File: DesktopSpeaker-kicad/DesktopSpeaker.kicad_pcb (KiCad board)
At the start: 4 copper layers, 127.5 x 137.6 mm, 360 parts, among them J1 USB_C_Receptacle_USB2.0_16P, J10 B2P-VH, J11 B2P-VH, J2 HEAD_OUT, J3 AUX_IN, J4 I2C service, J5 1S_PACK_3PIN, J6 SWD, J7 SWD_TC2030, J8 BM83_PROG, J9 B2P-VH, Q100 2N7002, Q101 2N7002, Q102 2N7002, Q103 CSD17579Q3A, Q104 2N7002, SW100 WAKE_QON, SW101 BAT_DISCONNECT, SW102 EC11E, U1 BM83SM1-00TA, U10 TPA6132A2RTER, U11 TPS25730DREFR, U12 TPS7A0230PDBVR, U13 TS5A3167DBVR, U14 TPS63802DLAR, U15 TPS63802DLAR, U16 TS5A3167DBVR, U17 TS5A3167DBVR, U19 TPS7B8450QWDRBRQ1, U2 PCM2902CDBR, U20 TPS2116DRLR, U21 TPS3839G33DBZR, U22 TPS7A2033PDBVR, U23 TPS22917DBVR, U24 PCM1862DBTR, U25 TPS61088RHLR, U3 STM32G071RBT6, U4 BQ25792RQMR, U5 MAX17048G+T10, U6 TAS5825MRHBR, U7 TAS5825MRHBR, U8 TS5A23157DGSR, U9 TS5A23157DGSR, Y170 12MHz, Y200 24.576MHz

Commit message: R6o adopted: DRC 0/0 (silk cleared, USB FS waiver rule, audio GND vias), library silk fixes, ignore intermediate boards
Co-Authored-By: Claude Fable 5.1 <noreply@anthropic.com>
Claude-Session: https://claude.ai/code/session_016fe4xPJbEE2SjGafuyNLjb
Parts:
- moved LOGO1 80.0 mm to (173.2, 55.1)
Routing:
- net /3V3_AUDIO: track 299.6 -> 301.9 mm
- net GND: vias 270 -> 272

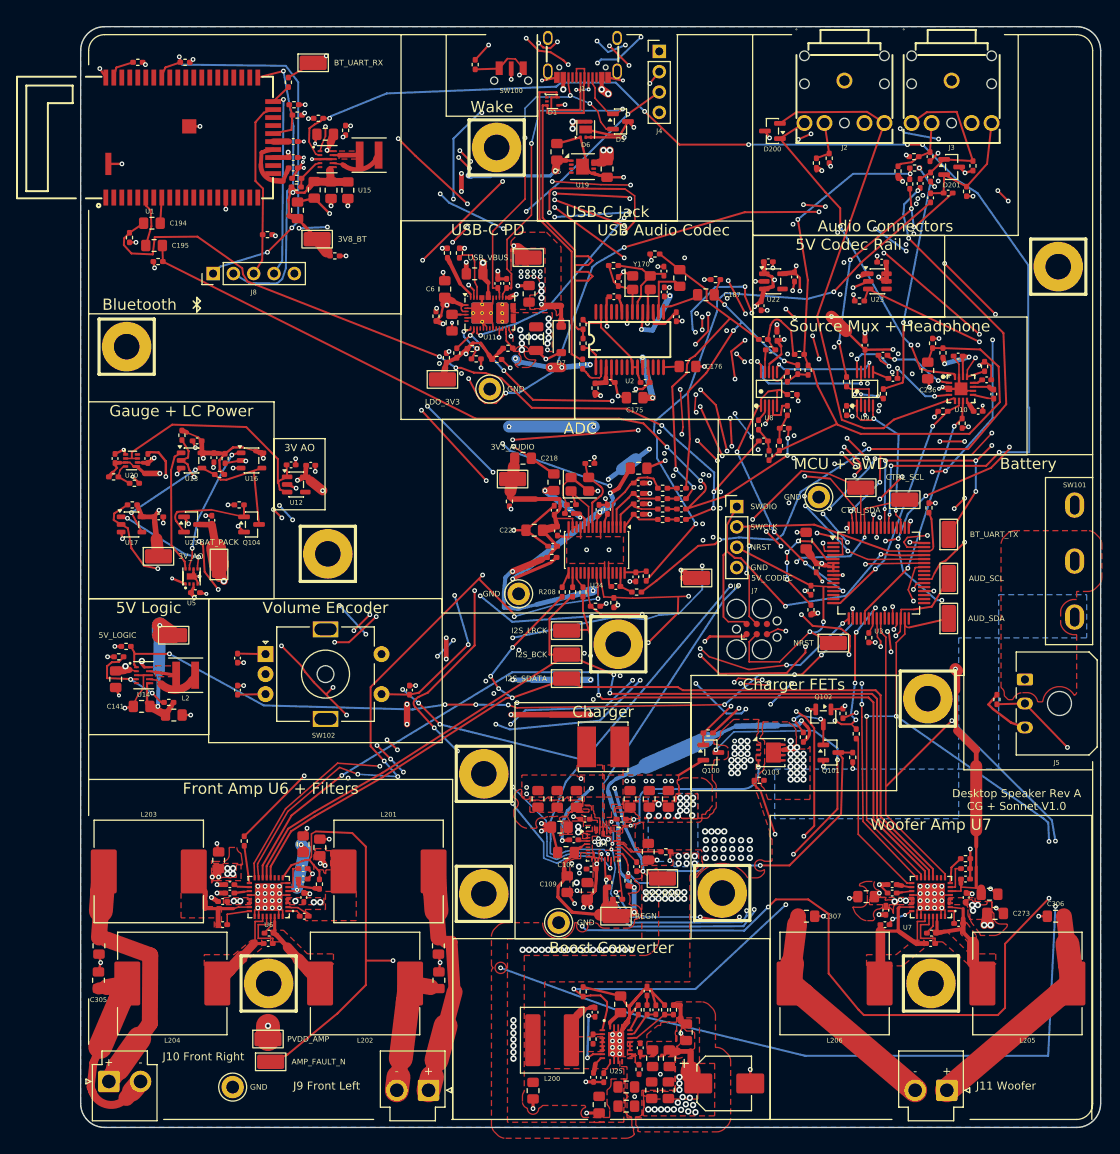
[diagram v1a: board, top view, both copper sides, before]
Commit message: R6p adopted: slow-signal geometry cleanup (16 nets shortened, -75 vias), teardrop strip/prune tools, fab export helper
- Project board = R6p-final: DRC 0/0, 0 open edges, USB/I2S copper and footprints unchanged vs R6o; rules unchanged.
- GUI teardrop pass of 2026-10-11 stripped (stale fills caused the 499 clearance items); U14-L2 GUI polyline redraw reverted to the 1.0 mm arc; td_curve_segcount back to 5.
- helpers: route_td_strip.py, route_td_prune.py, route_r6p_geom/improve/cucmp/netsvg/try/dangle.py, fab_export.sh (gerbers, drills, JLC CPL).
- .gitignore: KiCad local history, stray plugin log, work-r6 prl files, R6p finals tracked.
- Handover: R6p update and revised remaining fab steps.

Co-Authored-By: Claude Fable 5.1 <noreply@anthropic.com>
Claude-Session: https://claude.ai/code/session_016fe4xPJbEE2SjGafuyNLjb
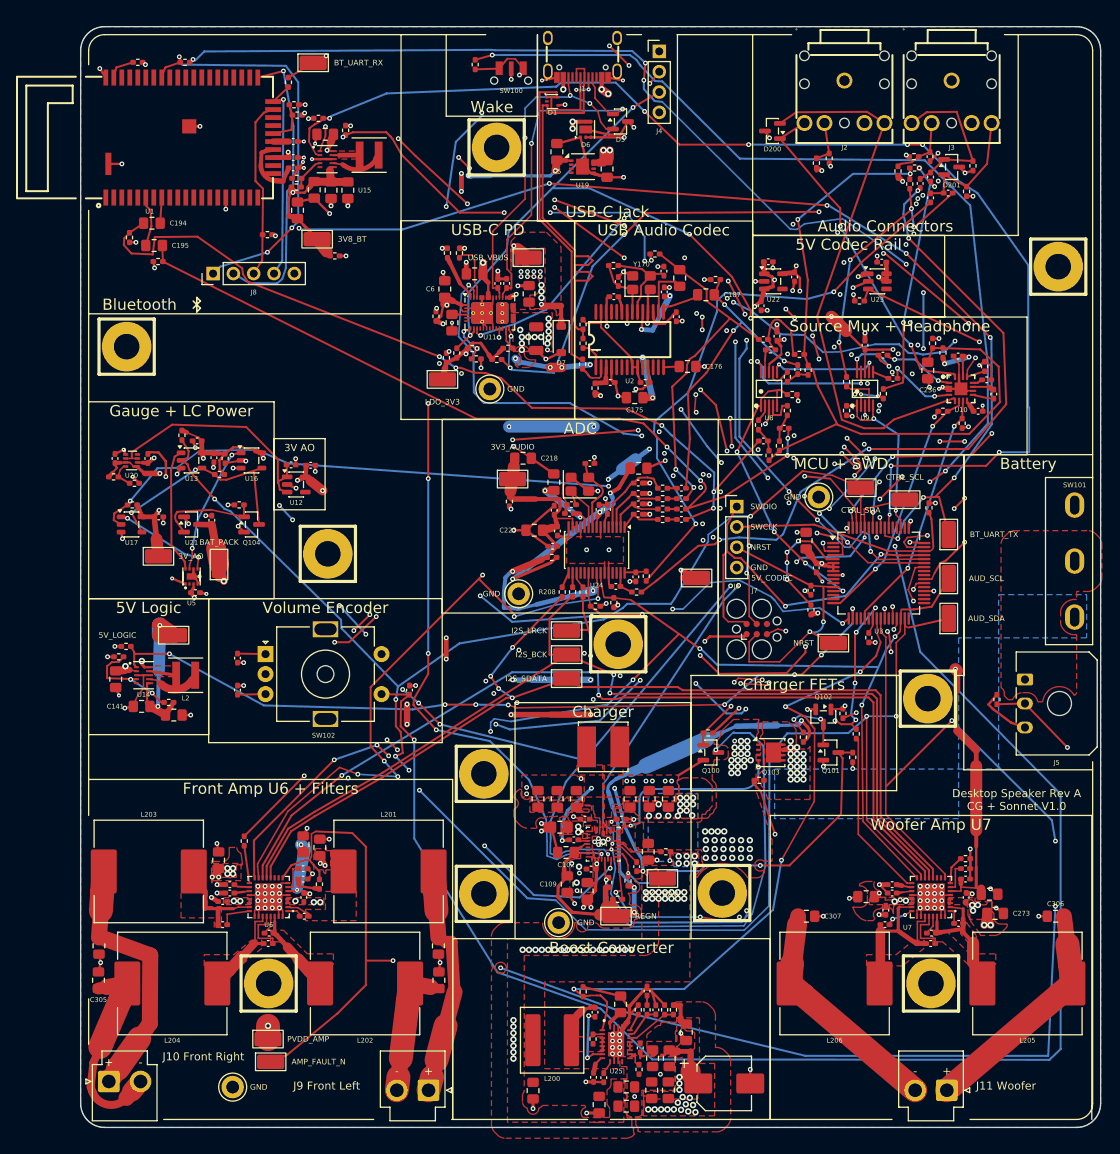
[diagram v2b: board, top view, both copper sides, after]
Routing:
- net /AUD_SDA: track 277.9 -> 220.3 mm, vias 13 -> 10
- net /BT_RST_N: track 187.2 -> 141.2 mm
- net /PDCTRL_SDA: track 148.5 -> 122.8 mm, vias 16 -> 8
- net /PD_PLUG_EVENT: track 105.4 -> 80.4 mm, vias 13 -> 6
- net /PD_SINK_EN: track 134.2 -> 119.1 mm, vias 11 -> 9
- net /Battery_Charger/CE_N: track 68.1 -> 55.3 mm, vias 5 -> 2
- net /BT_UART_TX: track 146.3 -> 134.9 mm, vias 18 -> 9
- net /MCU/ENC_SW: track 203.5 -> 193.7 mm, vias 17 -> 3
- net /BT_PWR_EN: track 140.4 -> 130.7 mm, vias 7 -> 8
- net /CTRL_SDA: track 172.2 -> 162.7 mm, vias 16 -> 7
- net /GAUGE_ALRT_N: track 119.0 -> 110.1 mm, vias 8 -> 4
- net Net-(U4-QON): track 135.5 -> 126.9 mm, vias 10 -> 8
- net /PDCTRL_SCL: track 124.1 -> 116.9 mm, vias 13 -> 10
- net /AMP_BOOST_EN: track 88.3 -> 83.2 mm, vias 7 -> 4
- net /CHG_QON_SENSE: track 135.0 -> 130.0 mm, vias 13 -> 6
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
